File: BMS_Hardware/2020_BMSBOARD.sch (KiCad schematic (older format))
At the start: 26 parts

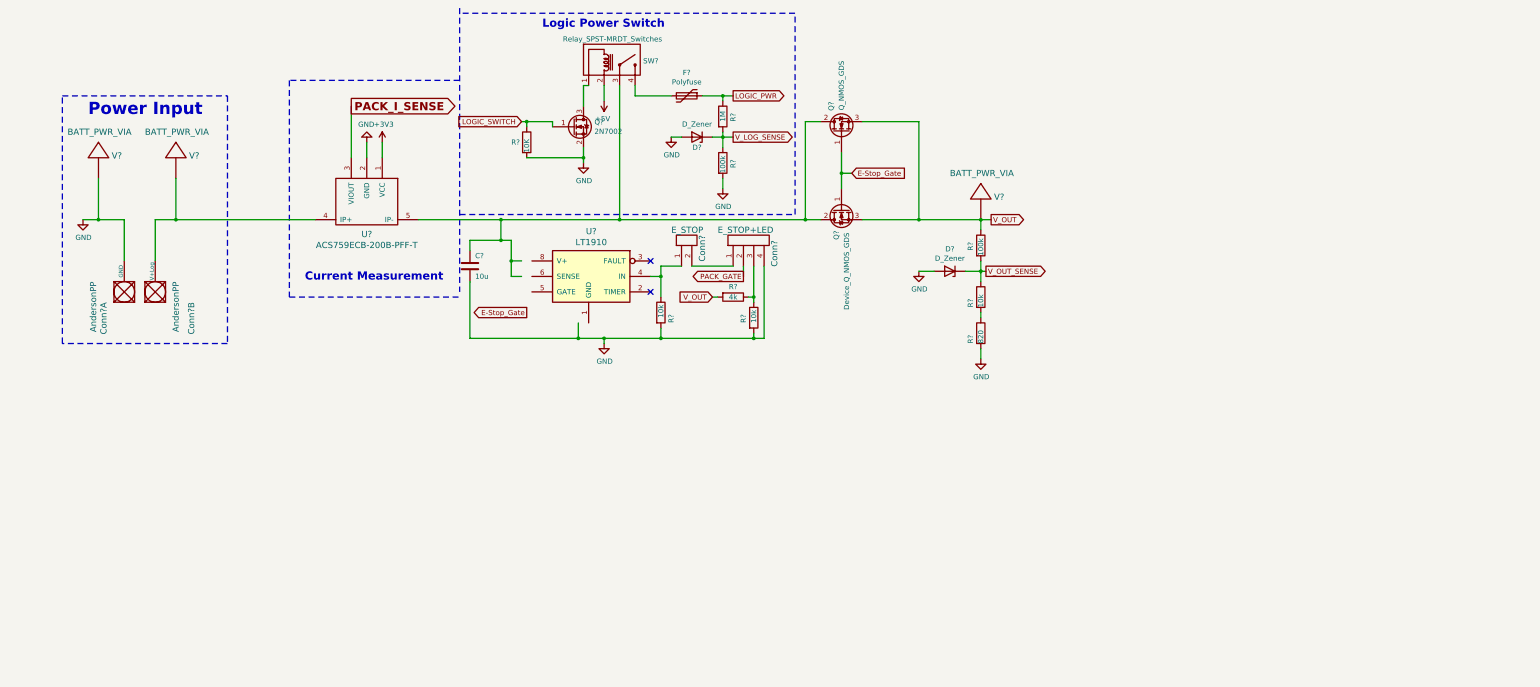
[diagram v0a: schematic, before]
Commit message: schematic almost done
Still planning how to change diffops amps and currently putting in microcontroller
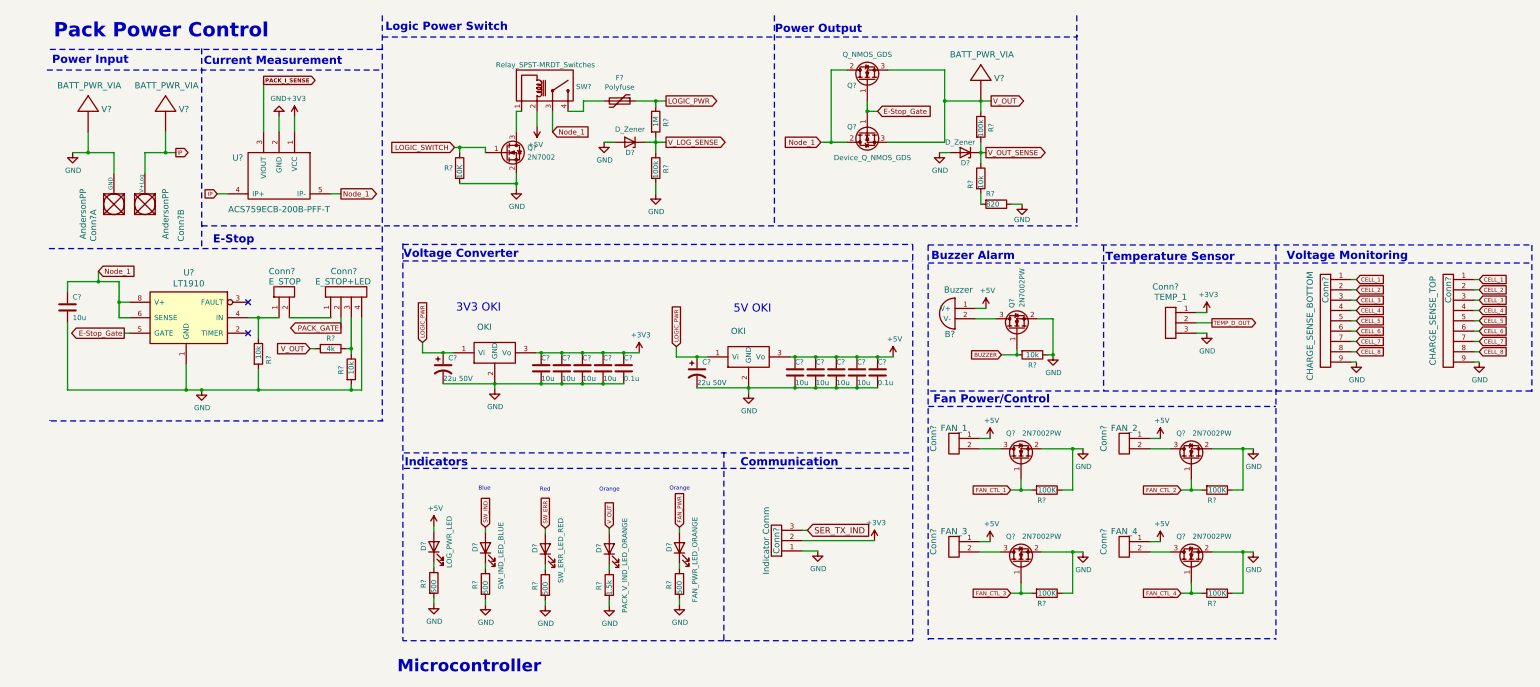
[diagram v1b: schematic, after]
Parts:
- added B?: Buzzer, symbol MRDT_Devices:Buzzer
- added C? (x2): 22u 50V, symbol Device:CP1
- added C? (x8): 10u, symbol Device:C
- added C? (x2): 0.1u, symbol Device:C
- added Conn?: Indicator Comm, symbol BMS_Hardware-rescue:Molex_SL_03-MRDT_Connectors
- added Conn?: CHARGE_SENSE_BOTTOM, symbol BMS_Hardware-rescue:Molex_SL_09-MRDT_Connectors
- added Conn?: CHARGE_SENSE_TOP, symbol BMS_Hardware-rescue:Molex_SL_09-MRDT_Connectors
- added Conn?: TEMP_1, symbol MRDT_Connectors:Molex_SL_03
- added Conn?: FAN_1, symbol MRDT_Connectors:Molex_SL_02
- added Conn?: FAN_2, symbol MRDT_Connectors:Molex_SL_02
- added Conn?: FAN_3, symbol MRDT_Connectors:Molex_SL_02
- added Conn?: FAN_4, symbol MRDT_Connectors:Molex_SL_02
- added D?: LOG_PWR_LED, symbol Device:LED
- added D?: SW_IND_LED_BLUE, symbol Device:LED
- added D?: SW_ERR_LED_RED, symbol Device:LED
- added D?: PACK_V_IND_LED_ORANGE, symbol Device:LED
- added D?: FAN_PWR_LED_ORANGE, symbol Device:LED
- added Q? (x5): 2N7002PW, Package_TO_SOT_SMD:SOT-23, symbol BMS_Hardware-cache:2N7002
- added R? (x4): 500, symbol Device:R
- added R?: 1.5k, symbol Device:R
- added R?: 10k, symbol Device:R
- added R? (x4): 100K, symbol Device:R
- added U? (x2): OKI, symbol MRDT_Devices:OKI
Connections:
- net labels added: BUZZER, CELL_1, CELL_2, CELL_3, CELL_4, CELL_5, CELL_6, CELL_7, CELL_8, FAN_CTL_1, FAN_CTL_2, FAN_CTL_3, FAN_CTL_4, FAN_PWR, IP, Node_1, SER_TX_IND, SW_ERR, SW_IND, TEMP_D_OUT
- wire segments 84 -> 197
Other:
- note added: "3V3 OKI\n"
- note added: "5V OKI\n"
- note added: "Blue"
- note added: "Buzzer Alarm"
- note added: "Communication\n"
- note added: "E-Stop"
- note added: "Fan Power/Control"
- note added: "Indicators"
- note added: "Microcontroller"
- note added: "Orange\n"
- note added: "Pack Power Control"
- note added: "Power Output"
- note added: "Red"
- note added: "Temperature Sensor"
- note added: "Voltage Converter"
- note added: "Voltage Monitoring"
- moved on the sheet: C?, Conn?, Conn?A, Conn?B, D?, F?, Q?, R?, SW?, U?, V?

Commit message: added stuff
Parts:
- removed Conn?: AndersonPP, symbol MRDT_Connectors:AndersonPP
- added C?: 1u, symbol Device:C
- added Conn?: AndersonPP, symbol MRDT_Connectors:AndersonPP
- added D?: 7.5V, symbol Device:D_Zener
- added D?: D_Zener, symbol Device:D_Zener
- added R?: 10k, symbol Device:R
- added R?: 36.5k, symbol Device:R
- added U? (x2): TM4C129E_Launchpad, symbol MRDT_Shields:TM4C129E_Launchpad
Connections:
- net +5V: now also U?.+5V (B1_1)
- net CELL_1: now also C?.1, D?.1 (K), R?.2
- net GND: now also C?.2, D?.2 (A), D?.2 (A), R?.2, U?.GND (B1_2)
- net IP: no longer names the net of U?.4 (IP+), V?.1
- net IP: now also Conn?.4 (PV+)
- net Node_1 renamed PV
- new net CELL_1-GND_SENSE: D?.1 (K), R?.1, R?.1
- no-connect marks 2 -> 12
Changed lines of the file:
@@
-$EndComp
-$Comp
-L MRDT_Connectors:AndersonPP Conn?
-U 2 1 5D92AA1E
-P 1500 2400
-F 0 "Conn?" H 1550 2150 60  0000 R CNN
-F 1 "AndersonPP" H 1750 2300 60  0000 R CNN
-F 2 "" H 1350 1850 60  0001 C CNN
-F 3 "" H 1350 1850 60  0001 C CNN
-	2    1500 2400
-	0    -1   -1   0
 $EndComp
 $Comp
@@
 	1250 3550 1200 3550
 Text GLabel 3300 2200 2    50   Output ~ 0
-Node_1
+PV
 Wire Wire Line
 	3300 2200 3200 2200
 Text GLabel 950  2950 2    50   Input ~ 0
-Node_1
+PV
 Text Notes 2460 2690 2    79   ~ 16
 E-Stop
 Text Notes 2600 700  2    138  ~ 28
 Pack Power Control
-Text GLabel 1700 1800 2    39   Output ~ 0
-IP
-Text GLabel 2100 2200 0    39   Input ~ 0
-IP
 Wire Wire Line
 	2200 2200 2100 2200
@@
 	1600 1600 1600 1800
 Connection ~ 1600 1800
-Wire Wire Line
-	1600 1800 1700 1800
 Wire Wire Line
 	850  1600 850  1800
@@
 	8050 1700 7950 1700
 Text GLabel 7950 1700 0    50   Input ~ 0
-Node_1
+PV
 Wire Wire Line
 	8500 1400 8400 1400
@@
 	1    0    0    -1
 $EndComp
-Text GLabel 5350 1600 2    50   Input ~ 0
-Node_1
-Wire Wire Line
-	5350 1600 5350 1400
+Text GLabel 5350 1500 3    50   Input ~ 0
+PV
 Wire Wire Line
 	5850 1300 5650 1300
@@
 Wire Notes Line
 	3900 2680 3900 6530
-Text Notes 5240 6850 2    118  ~ 24
+Text Notes 5250 6750 2    118  ~ 24
 Microcontroller
+$Comp
+L MRDT_Shields:TM4C129E_Launchpad U?
+U 1 1 5E8F22FE
+P 4150 8150
+F 0 "U?" H 3850 9400 60  0000 L CNN
+F 1 "TM4C129E_Launchpad" H 3450 9300 60  0000 L CNN
+F 2 "" H 4150 8150 60  0001 C CNN
+F 3 "" H 4150 8150 60  0001 C CNN
+	1    4150 8150
+	1    0    0    -1
+$EndComp
+NoConn ~ 3950 7200
+NoConn ~ 3950 7300
+NoConn ~ 3950 7400
+NoConn ~ 3950 7500
+NoConn ~ 3950 7600
+NoConn ~ 3950 7700
+NoConn ~ 3950 7800
+NoConn ~ 3950 7900
+NoConn ~ 3950 8000
+NoConn ~ 3950 8100
+$Comp
+L MRDT_Shields:TM4C129E_Launchpad U?
+U 2 1 5E96159F
+P 4850 8150
+F 0 "U?" H 5000 9450 60  0000 C CNN
+F 1 "TM4C129E_Launchpad" H 4700 9350 60  0000 C CNN
+F 2 "" H 4850 8150 60  0001 C CNN
+F 3 "" H 4850 8150 60  0001 C CNN
+	2    4850 8150
+	-1   0    0    -1
+$EndComp
+$Comp
+L power:+5V #PWR?
+U 1 1 5E968D7C
+P 5100 7200
+F 0 "#PWR?" H 5100 7050 50  0001 C CNN
+F 1 "+5V" H 5115 7373 50  0000 C CNN
+F 2 "" H 5100 7200 50  0001 C CNN
+F 3 "" H 5100 7200 50  0001 C CNN
+	1    5100 7200
+	1    0    0    -1
+$EndComp
+Wire Wire Line
+	5050 7200 5100 7200
+$Comp
+L power:GND #PWR?
+U 1 1 5E975735
+P 5150 7300
+F 0 "#PWR?" H 5150 7050 50  0001 C CNN
+F 1 "GND" V 5155 7172 50  0000 R CNN
+F 2 "" H 5150 7300 50  0001 C CNN
+F 3 "" H 5150 7300 50  0001 C CNN
+	1    5150 7300
+	0    -1   -1   0
+$EndComp
+Text GLabel 750  4500 0    39   Input ~ 0
+CELL_8
+Text GLabel 750  4700 0    39   Input ~ 0
+CELL_7
+Text GLabel 750  4900 0    39   Input ~ 0
+CELL_6
+Text GLabel 750  5100 0    39   Input ~ 0
+CELL_5
+Text GLabel 750  5300 0    39   Input ~ 0
+CELL_4
+Text GLabel 750  5500 0    39   Input ~ 0
+CELL_3
+Text GLabel 750  5700 0    39   Input ~ 0
+CELL_2
+Text GLabel 750  6350 0    39   Input ~ 0
+CELL_1
+Wire Wire Line
+	750  6350 950  6350
+$Comp
+L Device:C C?
+U 1 1 5EA0D5EF
+P 950 6550
+F 0 "C?" H 850 6450 50  0000 L CNN
+F 1 "1u" H 850 6650 50  0000 L CNN
+F 2 "" H 988 6400 50  0001 C CNN
+F 3 "~" H 950 6550 50  0001 C CNN
+	1    950  6550
+	1    0    0    -1
+$EndComp
+Wire Wire Line
+	950  6350 950  6400
+Wire Wire Line
+	950  6700 950  6750
+Wire Wire Line
+	950  6750 1150 6750
+Wire Wire Line
+	1350 6750 1350 6700
+$Comp
+L power:GND #PWR?
+U 1 1 5EA25801
+P 1150 6750
+F 0 "#PWR?" H 1150 6500 50  0001 C CNN
+F 1 "GND" H 1155 6577 50  0000 C CNN
+F 2 "" H 1150 6750 50  0001 C CNN
+F 3 "" H 1150 6750 50  0001 C CNN
+	1    1150 6750
+	1    0    0    -1
+$EndComp
+Connection ~ 1150 6750
+Wire Wire Line
+	1150 6750 1350 6750
+$Comp
+L Device:D_Zener D?
+U 1 1 5EA26AE2
+P 1350 6550
+F 0 "D?" H 1300 6650 50  0000 L CNN
+F 1 "7.5V" H 1250 6450 50  0000 L CNN
+F 2 "" H 1350 6550 50  0001 C CNN
+F 3 "~" H 1350 6550 50  0001 C CNN
+	1    1350 6550
+	0    1    1    0
+$EndComp
+Wire Wire Line
+	950  6350 1350 6350
+Wire Wire Line
+	1350 6350 1350 6400
+Connection ~ 950  6350
+$Comp
+L Device:R R?
+U 1 1 5EA34941
+P 1600 6350
+F 0 "R?" V 1700 6400 50  0000 C CNN
+F 1 "10k" V 1600 6350 50  0000 C CNN
+F 2 "" V 1530 6350 50  0001 C CNN
+F 3 "~" H 1600 6350 50  0001 C CNN
+	1    1600 6350
+	0    1    1    0
+$EndComp
+Wire Wire Line
+	1350 6350 1450 6350
+Connection ~ 1350 6350
+Wire Wire Line
+	1750 6350 1850 6350
+Wire Wire Line
+	1850 6350 1850 6400
+Connection ~ 1850 6350
+$Comp
+L Device:D_Zener D?
+U 1 1 5EA66203
+P 1850 6550
+F 0 "D?" H 1800 6650 50  0000 L CNN
+F 1 "D_Zener" H 1750 6450 50  0000 L CNN
+F 2 "" H 1850 6550 50  0001 C CNN
+F 3 "~" H 1850 6550 50  0001 C CNN
+	1    1850 6550
+	0    1    1    0
+$EndComp
+$Comp
+L power:GND #PWR?
+U 1 1 5EA7276D
+P 1850 6750
+F 0 "#PWR?" H 1850 6500 50  0001 C CNN
+F 1 "GND" H 1855 6577 50  0000 C CNN
+F 2 "" H 1850 6750 50  0001 C CNN
+F 3 "" H 1850 6750 50  0001 C CNN
+	1    1850 6750
+	1    0    0    -1
+$EndComp
+$Comp
+L power:GND #PWR?
+U 1 1 5EA72D43
+P 2100 6750
+F 0 "#PWR?" H 2100 6500 50  0001 C CNN
+F 1 "GND" H 2105 6577 50  0000 C CNN
+F 2 "" H 2100 6750 50  0001 C CNN
+F 3 "" H 2100 6750 50  0001 C CNN
+	1    2100 6750
+	1    0    0    -1
+$EndComp
+Wire Wire Line
+	1850 6700 1850 6750
+$Comp
+L MRDT_Connectors:AndersonPP Conn?
+U 4 1 5EAA3DB1
+P 1500 2400
+F 0 "Conn?" H 1550 2250 60  0000 R CNN
+F 1 "AndersonPP" H 1750 2350 60  0000 R CNN
+F 2 "" H 1350 1850 60  0001 C CNN
+F 3 "" H 1350 1850 60  0001 C CNN
+	4    1500 2400
+	0    -1   -1   0
+$EndComp
+Wire Wire Line
+	2100 1800 2100 2200
+Wire Wire Line
+	1600 1800 2100 1800
+Wire Wire Line
+	5350 1400 5350 1500
+Wire Wire Line
+	5050 7300 5150 7300
+$Comp
+L Device:R R?
+U 1 1 5EAEE814
+P 2100 6550
+F 0 "R?" V 2200 6550 50  0000 L CNN
+F 1 "36.5k" V 2100 6450 50  0000 L CNN
+F 2 "" V 2030 6550 50  0001 C CNN
+F 3 "~" H 2100 6550 50  0001 C CNN
+	1    2100 6550
+	1    0    0    -1
+$EndComp
+Wire Wire Line
+	2100 6350 2100 6400
+Wire Wire Line
+	2100 6700 2100 6750
+Wire Wire Line
+	1850 6350 2100 6350
+Wire Wire Line
+	2100 6350 2300 6350
+Connection ~ 2100 6350
+Text GLabel 2300 6350 2    39   Output ~ 0
+CELL_1-GND_SENSE
 $EndSCHEMATC

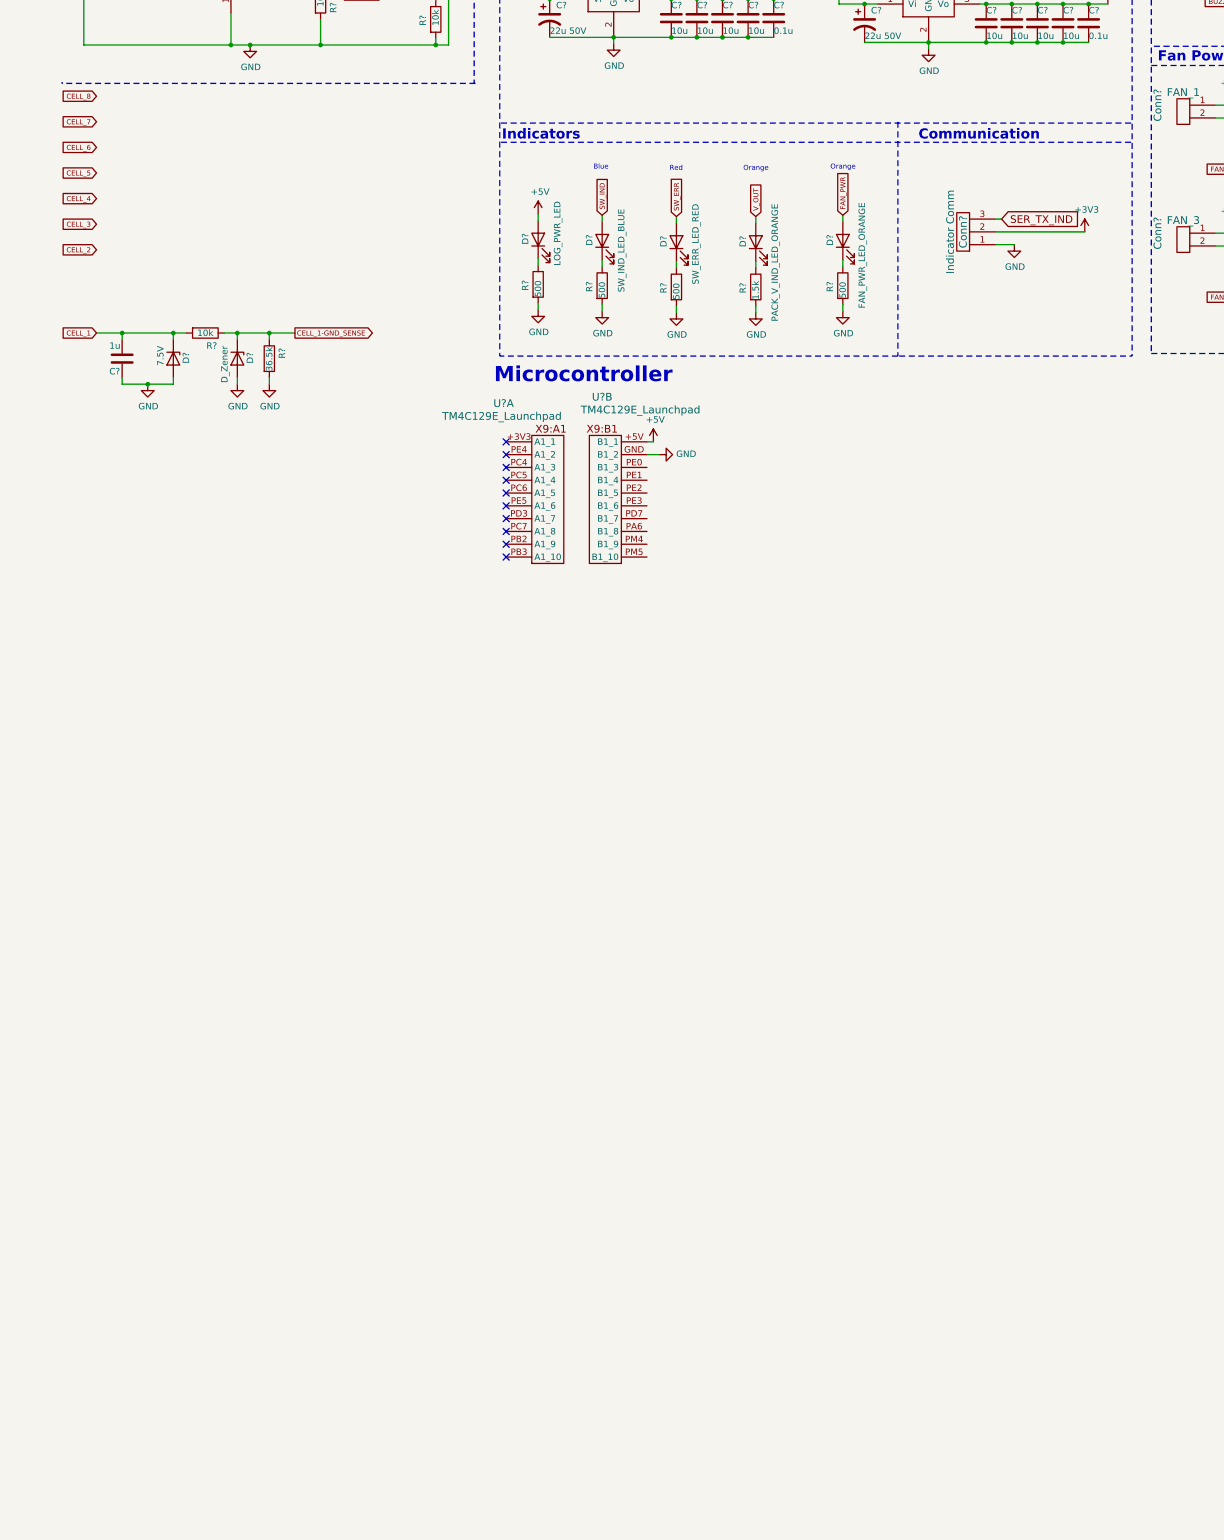
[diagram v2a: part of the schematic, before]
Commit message: schematic almost done
Just need microcontroller pinouts and we changed the diffop amps to op amps with resisters
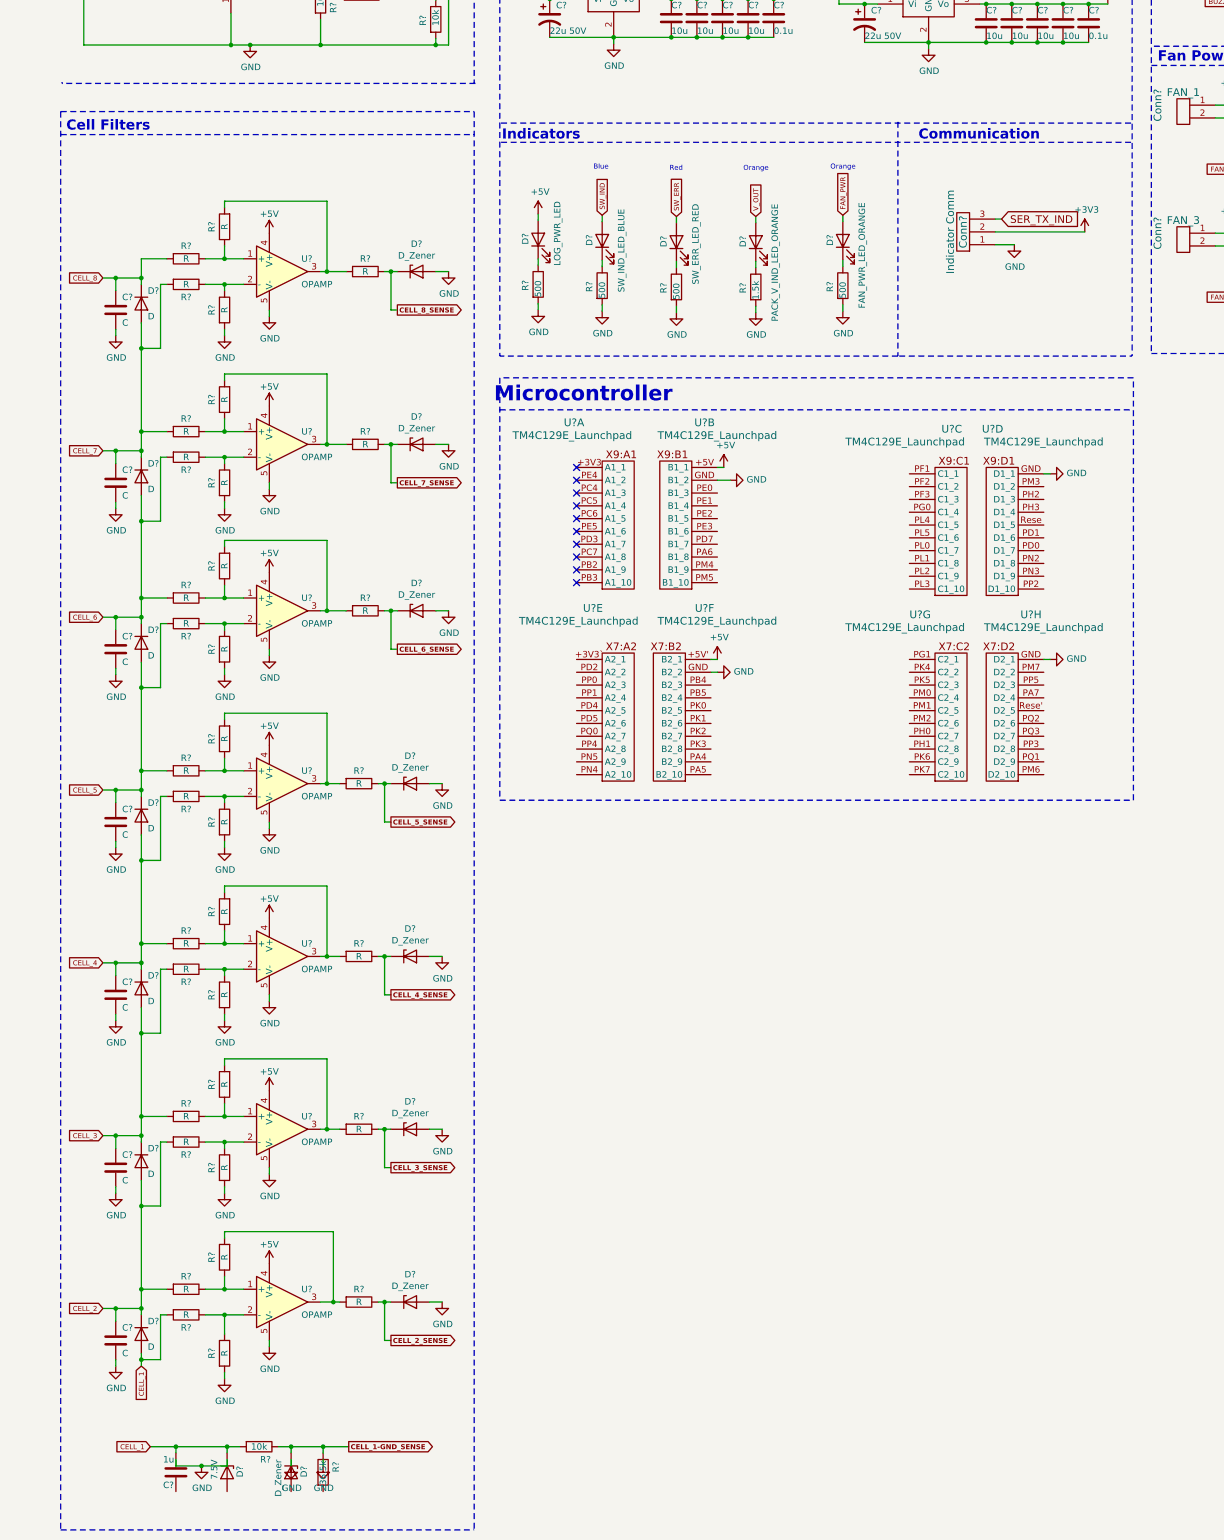
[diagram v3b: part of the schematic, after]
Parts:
- added C? (x7): C, symbol Device:C
- added D? (x7): D, symbol Device:D
- added D? (x7): D_Zener, symbol Device:D_Zener
- added R? (x35): R, symbol Device:R
- added U? (x6): TM4C129E_Launchpad, symbol MRDT_Shields:TM4C129E_Launchpad
- added U? (x7): OPAMP, symbol pspice:OPAMP
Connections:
- net +5V: now also U?.+5V' (B2_1), U?.4 (V+), U?.4 (V+), U?.4 (V+), U?.4 (V+), U?.4 (V+), U?.4 (V+), U?.4 (V+)
- net CELL_1: now also D?.2 (A), R?.2
- net CELL_2: now also C?.1, D?.1 (K), D?.2 (A), R?.2, R?.2
- net CELL_3: now also C?.1, D?.1 (K), D?.2 (A), R?.2, R?.2
- net CELL_4: now also C?.1, D?.1 (K), D?.2 (A), R?.2, R?.2
- net CELL_5: now also C?.1, D?.1 (K), D?.2 (A), R?.2, R?.2
- net CELL_6: now also C?.1, D?.1 (K), D?.2 (A), R?.2, R?.2
- net CELL_7: now also C?.1, D?.1 (K), D?.2 (A), R?.2, R?.2
- net CELL_8: now also C?.1, D?.1 (K), R?.2
- net GND: now also C?.2, C?.2, C?.2, C?.2, C?.2, C?.2, C?.2, D?.2 (A), D?.2 (A), D?.2 (A), D?.2 (A), D?.2 (A), D?.2 (A), D?.2 (A), R?.2, R?.2, R?.2, R?.2, R?.2, R?.2, R?.2, U?.5 (V-), U?.5 (V-), U?.5 (V-), U?.5 (V-), U?.5 (V-), U?.5 (V-), U?.5 (V-), U?.GND (B2_2), U?.GND (D1_1), U?.GND (D2_1); no longer C?.2, D?.2 (A), D?.2 (A), R?.2
- new net: R?.1, R?.1, U?.1 (+) (x7)
- new net: R?.1, R?.1, U?.2 (-) (x7)
- new net: R?.2, R?.2, U?.3 (x7)
- new net CELL_2_SENSE: D?.1 (K), R?.1
- new net CELL_3_SENSE: D?.1 (K), R?.1
- new net CELL_4_SENSE: D?.1 (K), R?.1
- new net CELL_5_SENSE: D?.1 (K), R?.1
- new net CELL_6_SENSE: D?.1 (K), R?.1
- new net CELL_7_SENSE: D?.1 (K), R?.1
- new net CELL_8_SENSE: D?.1 (K), R?.1
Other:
- note added: "Cell Filters"
- moved on the sheet: C?, D?, R?, U?A, U?B
